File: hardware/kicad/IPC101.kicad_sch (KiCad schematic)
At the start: 0 parts

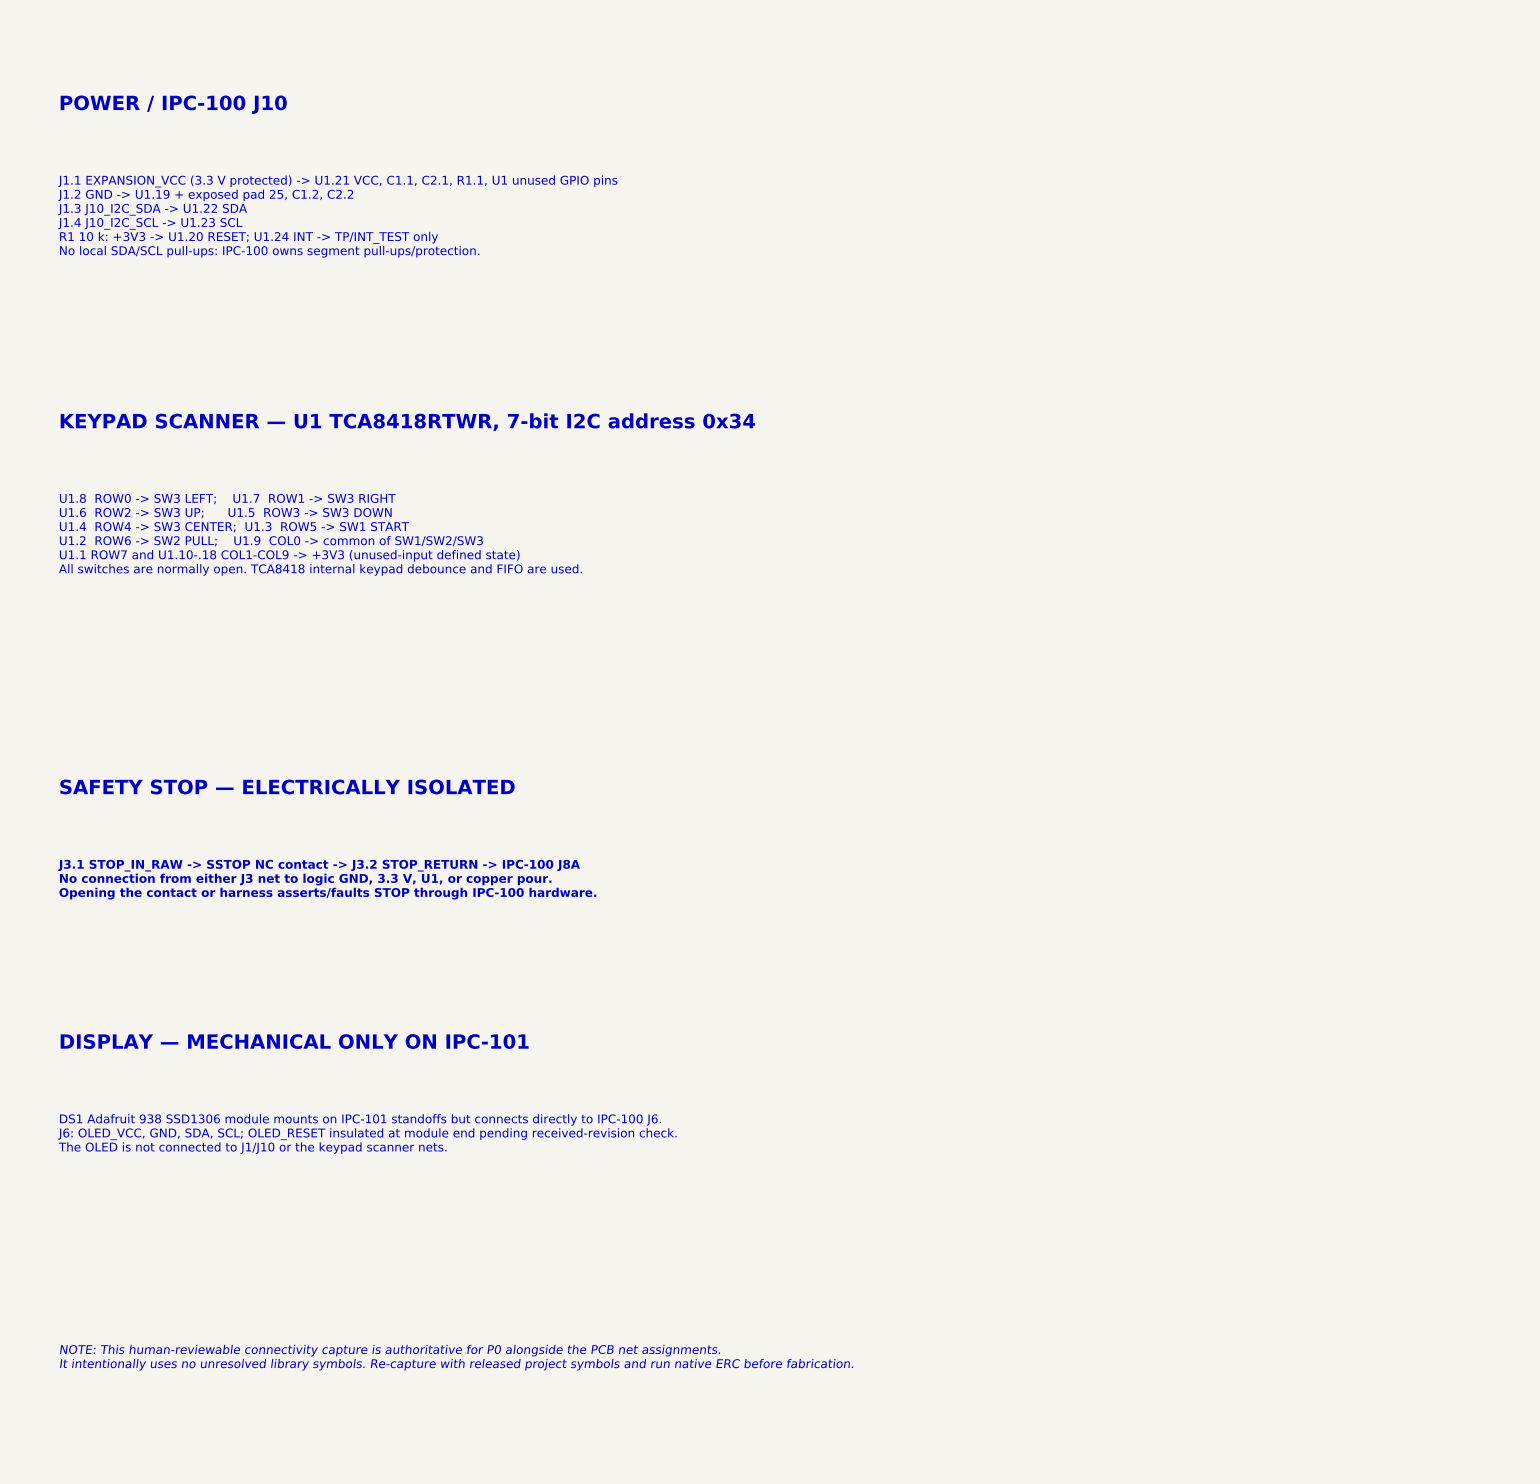
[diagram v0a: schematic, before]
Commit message: Add connected IPC-101 KiCad schematic
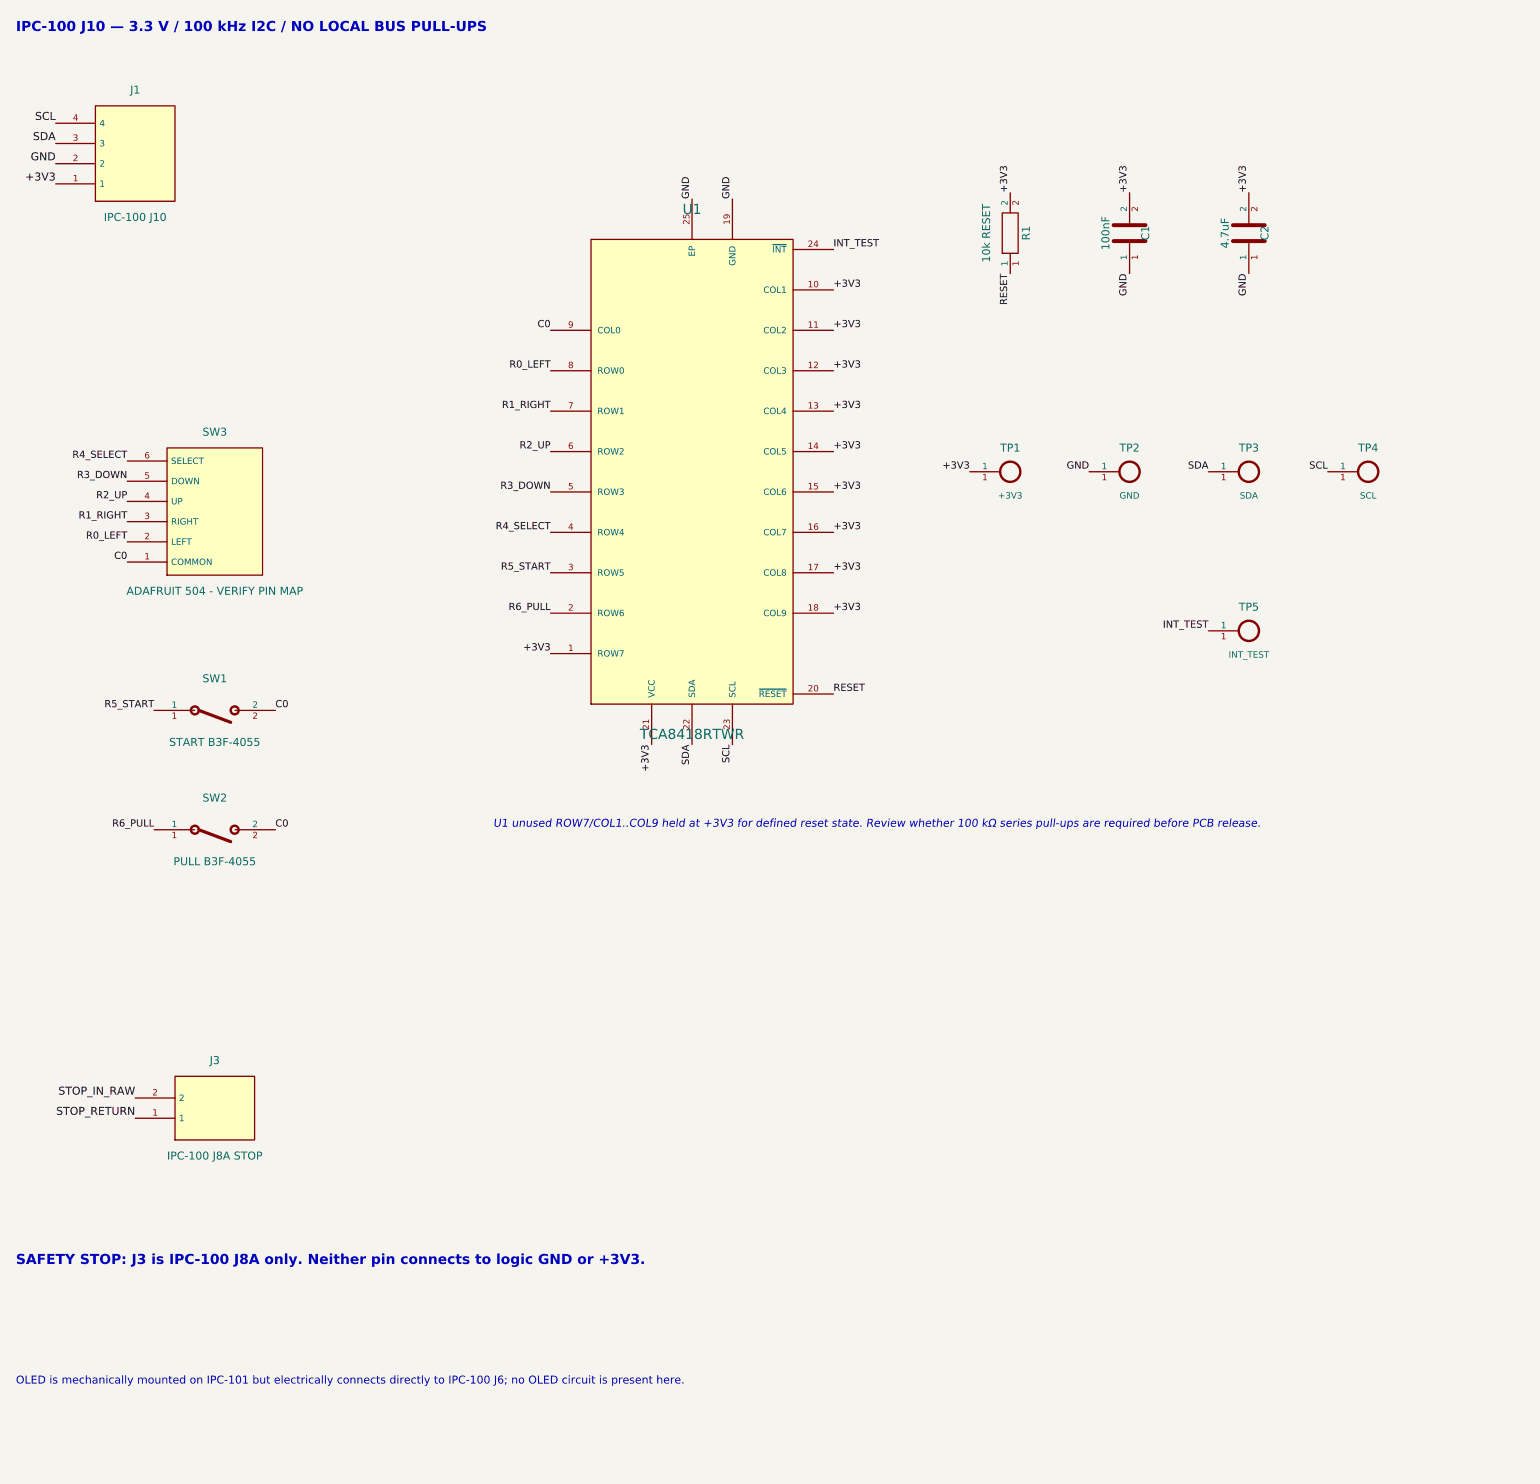
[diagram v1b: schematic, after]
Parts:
- added C1: 100nF, IPC101:C0805, symbol IPC101:C
- added C2: 4.7uF, IPC101:C0805, symbol IPC101:C
- added J1: IPC-100 J10, IPC101:JST_GH_04, symbol IPC101:CONN4
- added J3: IPC-100 J8A STOP, IPC101:STOP_CONN, symbol IPC101:CONN2
- added R1: 10k RESET, IPC101:R0805, symbol IPC101:R
- added SW1: START B3F-4055, IPC101:B3F-4055, symbol IPC101:SW2
- added SW2: PULL B3F-4055, IPC101:B3F-4055, symbol IPC101:SW2
- added SW3: ADAFRUIT 504 - VERIFY PIN MAP, IPC101:Adafruit_504_VERIFY, symbol IPC101:NAV6
- added TP1: +3V3, IPC101:TEST_LOOP, symbol IPC101:TP
- added TP2: GND, IPC101:TEST_LOOP, symbol IPC101:TP
- added TP3: SDA, IPC101:TEST_LOOP, symbol IPC101:TP
- added TP4: SCL, IPC101:TEST_LOOP, symbol IPC101:TP
- added TP5: INT_TEST, IPC101:TEST_LOOP, symbol IPC101:TP
- added U1: TCA8418RTWR, IPC101:TCA8418_RTW24, symbol IPC101:TCA8418
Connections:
- new net +3V3: C1.2, C2.2, J1.1, R1.2, TP1.1, U1.1 (ROW7), U1.10 (COL1), U1.11 (COL2), U1.12 (COL3), U1.13 (COL4), U1.14 (COL5), U1.15 (COL6), U1.16 (COL7), U1.17 (COL8), U1.18 (COL9), U1.21 (VCC)
- new net C0: SW1.2, SW2.2, SW3.1 (COMMON), U1.9 (COL0)
- new net GND: C1.1, C2.1, J1.2, TP2.1, U1.19 (GND), U1.25 (EP)
- new net INT_TEST: TP5.1, U1.24 (~{INT})
- new net R0_LEFT: SW3.2 (LEFT), U1.8 (ROW0)
- new net R1_RIGHT: SW3.3 (RIGHT), U1.7 (ROW1)
- new net R2_UP: SW3.4 (UP), U1.6 (ROW2)
- new net R3_DOWN: SW3.5 (DOWN), U1.5 (ROW3)
- new net R4_SELECT: SW3.6 (SELECT), U1.4 (ROW4)
- new net R5_START: SW1.1, U1.3 (ROW5)
- new net R6_PULL: SW2.1, U1.2 (ROW6)
- new net RESET: R1.1, U1.20 (~{RESET})
- new net SCL: J1.4, TP4.1, U1.23 (SCL)
- new net SDA: J1.3, TP3.1, U1.22 (SDA)
- new net STOP_IN_RAW: J3.2
- new net STOP_RETURN: J3.1
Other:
- note added: "IPC-100 J10 — 3.3 V / 100 kHz I2C / NO LOCAL BUS PULL-UPS"
- note added: "OLED is mechanically mounted on IPC-101 but electrically connects directly to IPC-100 J6; no OLED circuit is present here."
- note added: "SAFETY STOP: J3 is IPC-100 J8A only. Neither pin connects to logic GND or +3V3."
- note added: "U1 unused ROW7/COL1..COL9 held at +3V3 for defined reset state. Review whether 100 kΩ series pull-ups are required before PCB release."
- note removed: "DISPLAY — MECHANICAL ONLY ON IPC-101"
- note removed: "DS1 Adafruit 938 SSD1306 module mounts on IPC-101 standoffs but connects directly to IPC-100 J6. J6: OLED_VCC, GND, SDA, SCL; OLED_RESET insulated at module end pending received-revision check. The OLED is not connected to J1/J10 or the keypad scanner nets."
- note removed: "J1.1 EXPANSION_VCC (3.3 V protected) -> U1.21 VCC, C1.1, C2.1, R1.1, U1 unused GPIO pins J1.2 GND -> U1.19 + exposed pad 25, C1.2, C2.2 J1.3 J10_I2C_SDA -> U1.22 SDA J1.4 J10_I2C_SCL -> U1.23 SCL R1 10 k: +3V3 -> U1.20 RESET; U1.24 INT -> TP/INT_TEST only No local SDA/SCL pull-ups: IPC-100 owns segment pull-ups/protection."
- note removed: "J3.1 STOP_IN_RAW -> SSTOP NC contact -> J3.2 STOP_RETURN -> IPC-100 J8A No connection from either J3 net to logic GND, 3.3 V, U1, or copper pour. Opening the contact or harness asserts/faults STOP through IPC-100 hardware."
- note removed: "KEYPAD SCANNER — U1 TCA8418RTWR, 7-bit I2C address 0x34"
- note removed: "NOTE: This human-reviewable connectivity capture is authoritative for P0 alongside the PCB net assignments. It intentionally uses no unresolved library symbols. Re-capture with released project symbols and run native ERC before fabrication."
- note removed: "POWER / IPC-100 J10"
- note removed: "SAFETY STOP — ELECTRICALLY ISOLATED"
- note removed: "U1.8 ROW0 -> SW3 LEFT; U1.7 ROW1 -> SW3 RIGHT U1.6 ROW2 -> SW3 UP; U1.5 ROW3 -> SW3 DOWN U1.4 ROW4 -> SW3 CENTER; U1.3 ROW5 -> SW1 START U1.2 ROW6 -> SW2 PULL; U1.9 COL0 -> common of SW1/SW2/SW3 U1.1 ROW7 and U1.10-.18 COL1-COL9 -> +3V3 (unused-input defined state) All switches are normally open. TCA8418 internal keypad debounce and FIFO are used."

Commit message: Fix IPC-101 schematic PCB synchronization
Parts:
- removed TP5: INT_TEST, IPC101:TEST_LOOP, symbol IPC101:TP
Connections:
- net +3V3: now also C1.1, C2.1, R1.1; no longer C1.2, C2.2, R1.2
- net GND: now also C1.2, C2.2; no longer C1.1, C2.1
- net RESET: now also R1.2; no longer R1.1
- net STOP_IN_RAW: now also J3.1; no longer J3.2
- net STOP_RETURN: now also J3.2; no longer J3.1
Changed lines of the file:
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@@
   (symbol (lib_id "IPC101:R") (at 145 45 0) (unit 1) (exclude_from_sim no) (in_bom yes) (on_board yes) (dnp no)
     (property "Reference" "R1" (at 147 45 90) (effects (font (size 1 1)))) (property "Value" "10k RESET" (at 142 45 90) (effects (font (size 1 1)))) (property "Footprint" "IPC101:R0805" (at 145 45 0) (effects (font (size 1 1)) hide)) (property "Datasheet" "" (at 145 45 0) (effects (font (size 1 1)) hide)) (pin "1") (pin "2") (instances (project "IPC101" (path "/10100000-0000-4000-8000-000000000220" (reference "R1") (unit 1)))))
-  (label "+3V3" (at 145 39.92 90) (effects (font (size .9 .9)) (justify left bottom)))
-  (label "RESET" (at 145 50.08 270) (effects (font (size .9 .9)) (justify right bottom)))
+  (label "RESET" (at 145 39.92 90) (effects (font (size .9 .9)) (justify left bottom)))
+  (label "+3V3" (at 145 50.08 270) (effects (font (size .9 .9)) (justify right bottom)))
   (symbol (lib_id "IPC101:C") (at 160 45 0) (unit 1) (exclude_from_sim no) (in_bom yes) (on_board yes) (dnp no)
     (property "Reference" "C1" (at 162 45 90) (effects (font (size 1 1)))) (property "Value" "100nF" (at 157 45 90) (effects (font (size 1 1)))) (property "Footprint" "IPC101:C0805" (at 160 45 0) (effects (font (size 1 1)) hide)) (property "Datasheet" "" (at 160 45 0) (effects (font (size 1 1)) hide)) (pin "1") (pin "2") (instances (project "IPC101" (path "/10100000-0000-4000-8000-000000000230" (reference "C1") (unit 1)))))
-  (label "+3V3" (at 160 39.92 90) (effects (font (size .9 .9)) (justify left bottom)))
-  (label "GND" (at 160 50.08 270) (effects (font (size .9 .9)) (justify right bottom)))
+  (label "GND" (at 160 39.92 90) (effects (font (size .9 .9)) (justify left bottom)))
+  (label "+3V3" (at 160 50.08 270) (effects (font (size .9 .9)) (justify right bottom)))
   (symbol (lib_id "IPC101:C") (at 175 45 0) (unit 1) (exclude_from_sim no) (in_bom yes) (on_board yes) (dnp no)
     (property "Reference" "C2" (at 177 45 90) (effects (font (size 1 1)))) (property "Value" "4.7uF" (at 172 45 90) (effects (font (size 1 1)))) (property "Footprint" "IPC101:C0805" (at 175 45 0) (effects (font (size 1 1)) hide)) (property "Datasheet" "" (at 175 45 0) (effects (font (size 1 1)) hide)) (pin "1") (pin "2") (instances (project "IPC101" (path "/10100000-0000-4000-8000-000000000240" (reference "C2") (unit 1)))))
-  (label "+3V3" (at 175 39.92 90) (effects (font (size .9 .9)) (justify left bottom)))
-  (label "GND" (at 175 50.08 270) (effects (font (size .9 .9)) (justify right bottom)))
+  (label "GND" (at 175 39.92 90) (effects (font (size .9 .9)) (justify left bottom)))
+  (label "+3V3" (at 175 50.08 270) (effects (font (size .9 .9)) (justify right bottom)))
   (symbol (lib_id "IPC101:CONN2") (at 45 155 0) (unit 1) (exclude_from_sim no) (in_bom yes) (on_board yes) (dnp no)
     (property "Reference" "J3" (at 45 149 0) (effects (font (size 1 1)))) (property "Value" "IPC-100 J8A STOP" (at 45 161 0) (effects (font (size 1 1)))) (property "Footprint" "IPC101:STOP_CONN" (at 45 155 0) (effects (font (size 1 1)) hide)) (property "Datasheet" "" (at 45 155 0) (effects (font (size 1 1)) hide)) (pin "1") (pin "2") (instances (project "IPC101" (path "/10100000-0000-4000-8000-000000000250" (reference "J3") (unit 1)))))
-  (label "STOP_IN_RAW" (at 35 153.73 180) (effects (font (size 1 1)) (justify right bottom)))
-  (label "STOP_RETURN" (at 35 156.27 180) (effects (font (size 1 1)) (justify right bottom)))
+  (label "STOP_RETURN" (at 35 153.73 180) (effects (font (size 1 1)) (justify right bottom)))
+  (label "STOP_IN_RAW" (at 35 156.27 180) (effects (font (size 1 1)) (justify right bottom)))
   (symbol (lib_id "IPC101:TP") (at 145 75 0) (unit 1) (exclude_from_sim no) (in_bom yes) (on_board yes) (dnp no) (property "Reference" "TP1" (at 145 72 0) (effects (font (size 1 1)))) (property "Value" "+3V3" (at 145 78 0) (effects (font (size .8 .8)))) (property "Footprint" "IPC101:TEST_LOOP" (at 145 75 0) (effects (font (size 1 1)) hide)) (property "Datasheet" "" (at 145 75 0) (effects (font (size 1 1)) hide)) (pin "1") (instances (project "IPC101" (path "/10100000-0000-4000-8000-000000000260" (reference "TP1") (unit 1)))))
   (label "+3V3" (at 139.92 75 180) (effects (font (size .9 .9)) (justify right bottom)))
@@
   (symbol (lib_id "IPC101:TP") (at 190 75 0) (unit 1) (exclude_from_sim no) (in_bom yes) (on_board yes) (dnp no) (property "Reference" "TP4" (at 190 72 0) (effects (font (size 1 1)))) (property "Value" "SCL" (at 190 78 0) (effects (font (size .8 .8)))) (property "Footprint" "IPC101:TEST_LOOP" (at 190 75 0) (effects (font (size 1 1)) hide)) (property "Datasheet" "" (at 190 75 0) (effects (font (size 1 1)) hide)) (pin "1") (instances (project "IPC101" (path "/10100000-0000-4000-8000-000000000290" (reference "TP4") (unit 1)))))
   (label "SCL" (at 184.92 75 180) (effects (font (size .9 .9)) (justify right bottom)))
-  (symbol (lib_id "IPC101:TP") (at 175 95 0) (unit 1) (exclude_from_sim no) (in_bom yes) (on_board yes) (dnp no) (property "Reference" "TP5" (at 175 92 0) (effects (font (size 1 1)))) (property "Value" "INT_TEST" (at 175 98 0) (effects (font (size .8 .8)))) (property "Footprint" "IPC101:TEST_LOOP" (at 175 95 0) (effects (font (size 1 1)) hide)) (property "Datasheet" "" (at 175 95 0) (effects (font (size 1 1)) hide)) (pin "1") (instances (project "IPC101" (path "/10100000-0000-4000-8000-000000000300" (reference "TP5") (unit 1)))))
-  (label "INT_TEST" (at 169.92 95 180) (effects (font (size .9 .9)) (justify right bottom)))
   (sheet_instances (path "/" (page "1")))
 )

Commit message: Update IPC-101 for 2.42-inch OLED
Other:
- note added: "Hosyond 2.42-inch SSD1309 OLED (B0G2RFLG1L) is separately panel mounted on IPC-100 J6; qualify sample and measure mechanics."
- note removed: "OLED is mechanically mounted on IPC-101 but electrically connects directly to IPC-100 J6; no OLED circuit is present here."
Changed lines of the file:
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@@
   (text "U1 unused ROW7/COL1..COL9 held at +3V3 for defined reset state. Review whether 100 kΩ series pull-ups are required before PCB release." (at 80 120 0) (effects (font (size 1 1) (italic yes)) (justify left bottom)))
   (text "SAFETY STOP: J3 is IPC-100 J8A only. Neither pin connects to logic GND or +3V3." (at 20 175 0) (effects (font (size 1.27 1.27) (bold yes)) (justify left bottom)))
-  (text "OLED is mechanically mounted on IPC-101 but electrically connects directly to IPC-100 J6; no OLED circuit is present here." (at 20 190 0) (effects (font (size 1 1)) (justify left bottom)))
+  (text "Hosyond 2.42-inch SSD1309 OLED (B0G2RFLG1L) is separately panel mounted on IPC-100 J6; qualify sample and measure mechanics." (at 20 190 0) (effects (font (size 1 1)) (justify left bottom)))
   (symbol (lib_id "IPC101:CONN4") (at 35 35 0) (unit 1) (exclude_from_sim no) (in_bom yes) (on_board yes) (dnp no)
     (property "Reference" "J1" (at 35 27 0) (effects (font (size 1 1)))) (property "Value" "IPC-100 J10" (at 35 43 0) (effects (font (size 1 1)))) (property "Footprint" "IPC101:JST_GH_04" (at 35 35 0) (effects (font (size 1 1)) hide)) (property "Datasheet" "https://www.jst-mfg.com/product/pdf/eng/eGH.pdf" (at 35 35 0) (effects (font (size 1 1)) hide))

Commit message: Mount 2.42 inch OLED on IPC-101
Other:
- note added: "DS1 Hosyond 2.42-inch SSD1309 OLED is mounted on IPC-101 and uses a dedicated 5-wire harness to IPC-100 J6: OLED_VCC, GND, SDA, SCL, RESET."
- note removed: "Hosyond 2.42-inch SSD1309 OLED (B0G2RFLG1L) is separately panel mounted on IPC-100 J6; qualify sample and measure mechanics."
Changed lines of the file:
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@@
   (text "U1 unused ROW7/COL1..COL9 held at +3V3 for defined reset state. Review whether 100 kΩ series pull-ups are required before PCB release." (at 80 120 0) (effects (font (size 1 1) (italic yes)) (justify left bottom)))
   (text "SAFETY STOP: J3 is IPC-100 J8A only. Neither pin connects to logic GND or +3V3." (at 20 175 0) (effects (font (size 1.27 1.27) (bold yes)) (justify left bottom)))
-  (text "Hosyond 2.42-inch SSD1309 OLED (B0G2RFLG1L) is separately panel mounted on IPC-100 J6; qualify sample and measure mechanics." (at 20 190 0) (effects (font (size 1 1)) (justify left bottom)))
+  (text "DS1 Hosyond 2.42-inch SSD1309 OLED is mounted on IPC-101 and uses a dedicated 5-wire harness to IPC-100 J6: OLED_VCC, GND, SDA, SCL, RESET." (at 20 190 0) (effects (font (size 1 1)) (justify left bottom)))
   (symbol (lib_id "IPC101:CONN4") (at 35 35 0) (unit 1) (exclude_from_sim no) (in_bom yes) (on_board yes) (dnp no)
     (property "Reference" "J1" (at 35 27 0) (effects (font (size 1 1)))) (property "Value" "IPC-100 J10" (at 35 43 0) (effects (font (size 1 1)))) (property "Footprint" "IPC101:JST_GH_04" (at 35 35 0) (effects (font (size 1 1)) hide)) (property "Datasheet" "https://www.jst-mfg.com/product/pdf/eng/eGH.pdf" (at 35 35 0) (effects (font (size 1 1)) hide))
